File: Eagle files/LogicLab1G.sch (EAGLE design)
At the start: 153 parts, among them IC1 74AHC1G00DBV, IC10 74AHC1G00DBV, IC11 74AHC1G00DBV, IC12 74AHC1G00DBV, IC13 74AHC1G00DBV, IC14 74AHC1G00DBV, IC15 74AHC1G00DBV, IC16 74AHC1G00DBV, IC17 74AHC1G00DBV, IC2 74AHC1G00DBV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

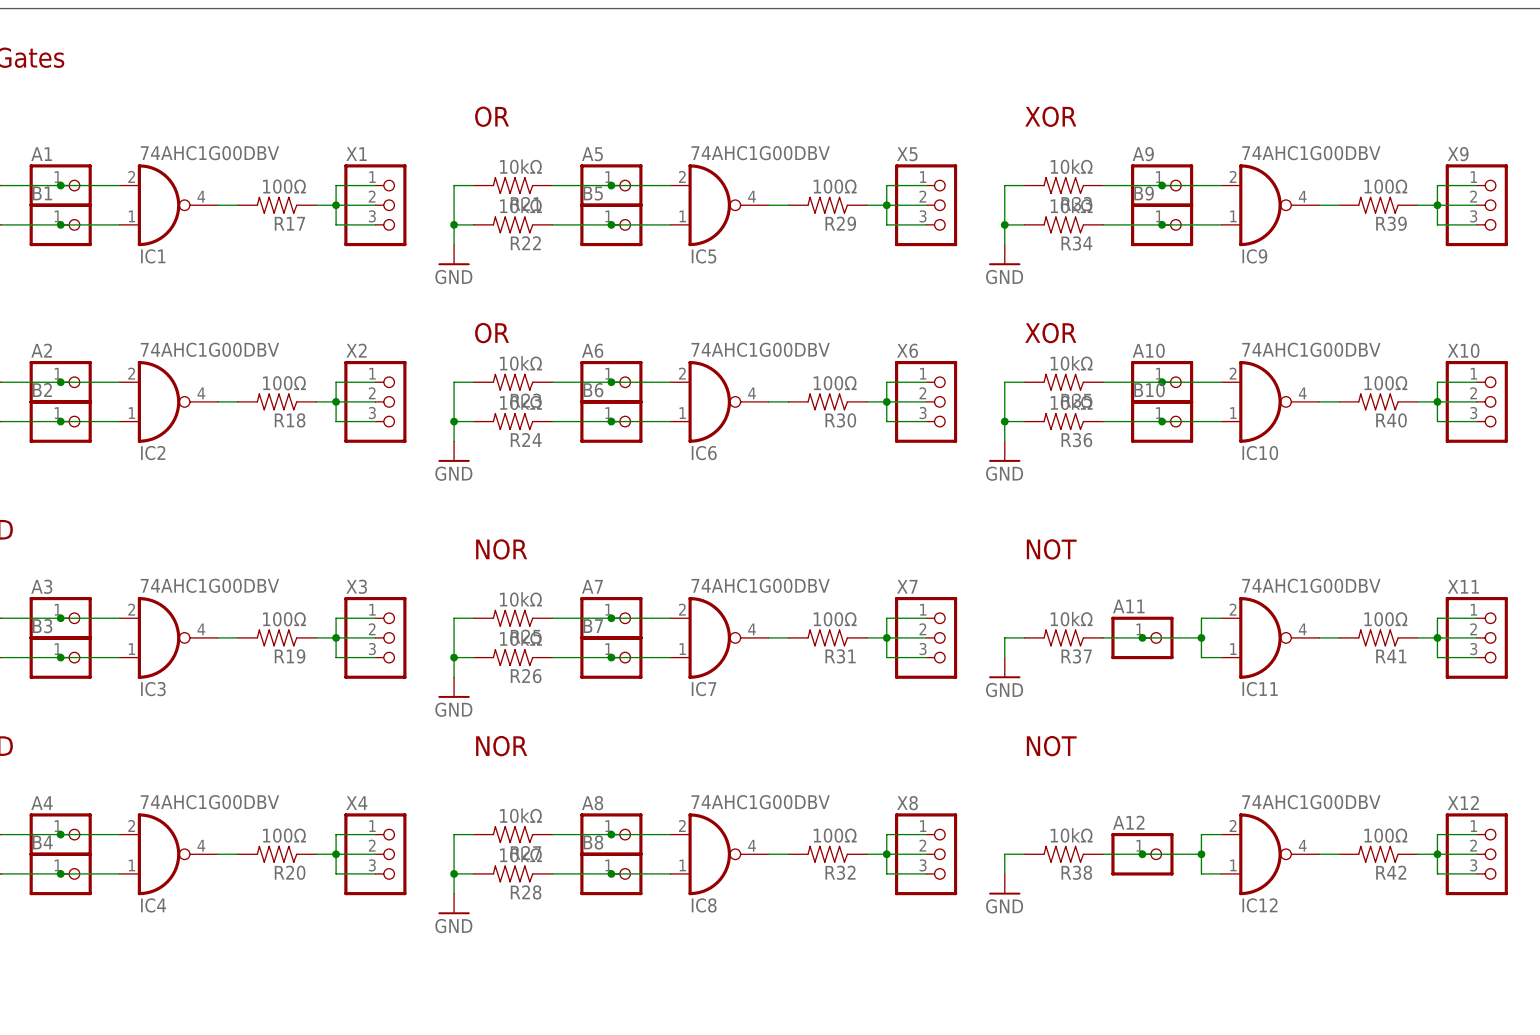
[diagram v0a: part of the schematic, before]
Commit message: Version 1a - 17th June 2024
Corrected the part numbers of the logic gates.
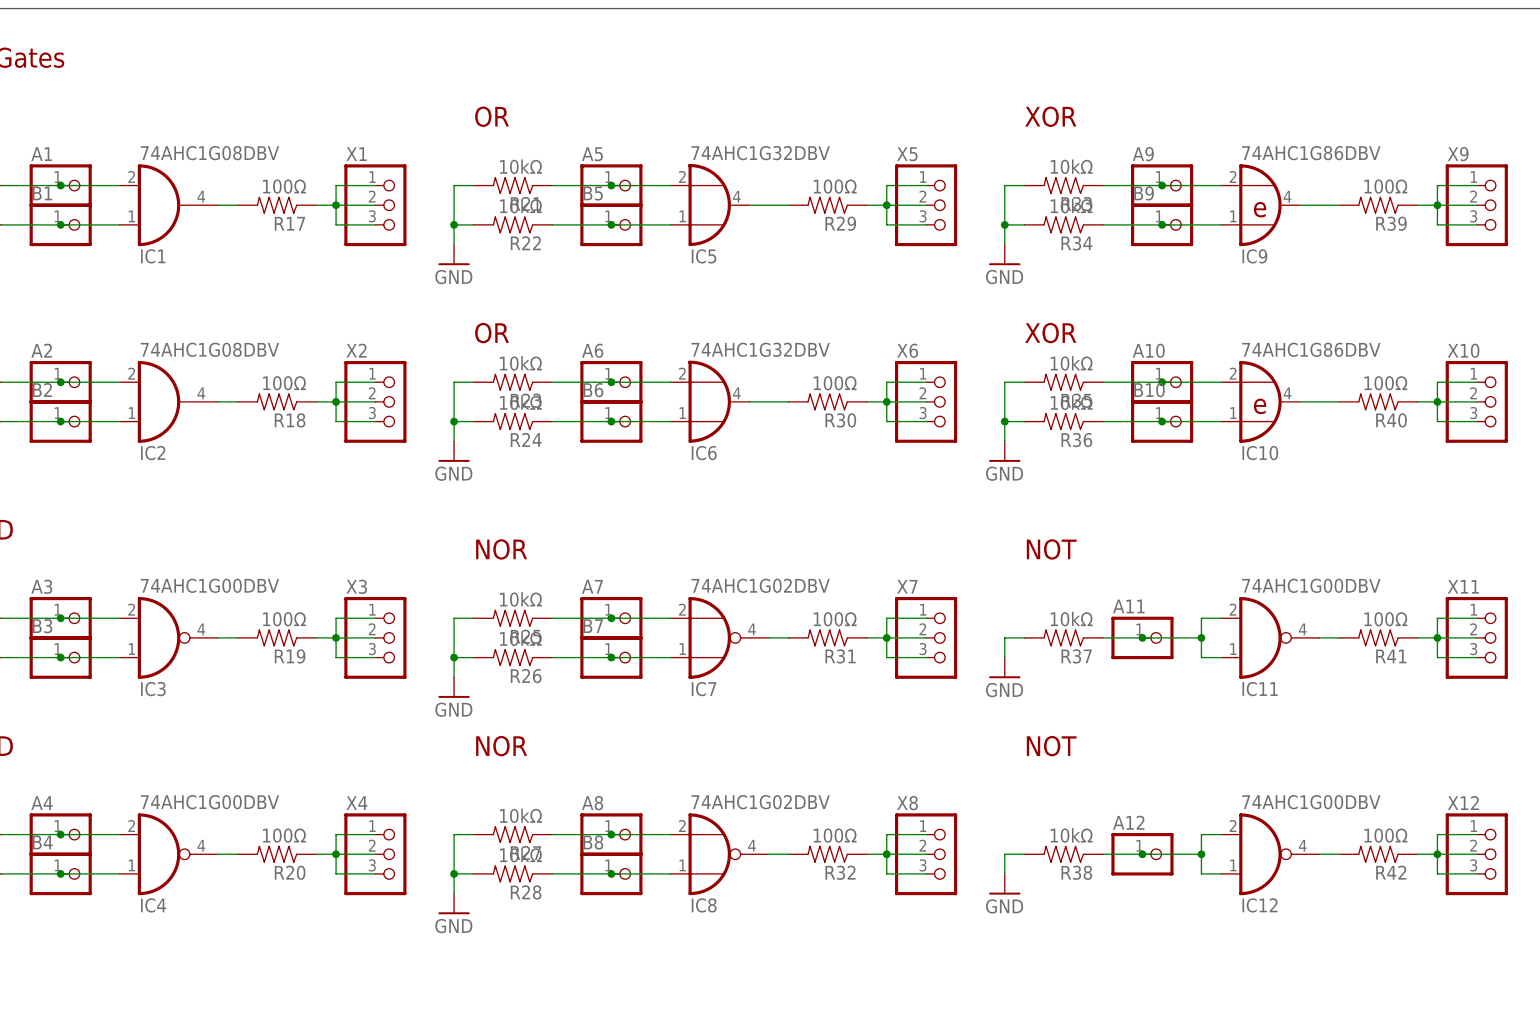
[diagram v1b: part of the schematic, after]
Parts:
- IC1, IC2: value 74AHC1G00DBV -> 74AHC1G08DBV; device 74xx-little-de:74AHC1G00DBV -> 74xx-little-de:74AHC1G08DBV
- IC10, IC9: value 74AHC1G00DBV -> 74AHC1G86DBV; device 74xx-little-de:74AHC1G00DBV -> 74xx-little-de:74AHC1G86DBV
- IC5, IC6: value 74AHC1G00DBV -> 74AHC1G32DBV; device 74xx-little-de:74AHC1G00DBV -> 74xx-little-de:74AHC1G32DBV
- IC7, IC8: value 74AHC1G00DBV -> 74AHC1G02DBV; device 74xx-little-de:74AHC1G00DBV -> 74xx-little-de:74AHC1G02DBV
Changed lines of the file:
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@@
 <part name="J1" library="adafruit" deviceset="1X4" device="-BIG"/>
 <part name="D1" library="SparkFun-DiscreteSemi" deviceset="B340A" device="" value="B340A"/>
-<part name="IC1" library="74xx-little-de" deviceset="74*1G00" device="DBV" technology="AHC"/>
-<part name="IC2" library="74xx-little-de" deviceset="74*1G00" device="DBV" technology="AHC"/>
+<part name="IC1" library="74xx-little-de" deviceset="74*1G08" device="DBV" technology="AHC"/>
+<part name="IC2" library="74xx-little-de" deviceset="74*1G08" device="DBV" technology="AHC"/>
 <part name="IC3" library="74xx-little-de" deviceset="74*1G00" device="DBV" technology="AHC"/>
 <part name="IC4" library="74xx-little-de" deviceset="74*1G00" device="DBV" technology="AHC"/>
-<part name="IC5" library="74xx-little-de" deviceset="74*1G00" device="DBV" technology="AHC"/>
-<part name="IC6" library="74xx-little-de" deviceset="74*1G00" device="DBV" technology="AHC"/>
-<part name="IC7" library="74xx-little-de" deviceset="74*1G00" device="DBV" technology="AHC"/>
-<part name="IC8" library="74xx-little-de" deviceset="74*1G00" device="DBV" technology="AHC"/>
-<part name="IC9" library="74xx-little-de" deviceset="74*1G00" device="DBV" technology="AHC"/>
-<part name="IC10" library="74xx-little-de" deviceset="74*1G00" device="DBV" technology="AHC"/>
+<part name="IC5" library="74xx-little-de" deviceset="74*1G32" device="DBV" technology="AHC"/>
+<part name="IC6" library="74xx-little-de" deviceset="74*1G32" device="DBV" technology="AHC"/>
+<part name="IC7" library="74xx-little-de" deviceset="74*1G02" device="DBV" technology="AHC"/>
+<part name="IC8" library="74xx-little-de" deviceset="74*1G02" device="DBV" technology="AHC"/>
+<part name="IC9" library="74xx-little-de" deviceset="74*1G86" device="DBV" technology="AHC"/>
+<part name="IC10" library="74xx-little-de" deviceset="74*1G86" device="DBV" technology="AHC"/>
 <part name="IC11" library="74xx-little-de" deviceset="74*1G00" device="DBV" technology="AHC"/>
 <part name="IC12" library="74xx-little-de" deviceset="74*1G00" device="DBV" technology="AHC"/>
@@
 <pinref part="IC5" gate="A" pin="O"/>
 <pinref part="R29" gate="G$1" pin="2"/>
-<wire x1="121.92" y1="124.46" x2="124.46" y2="124.46" width="0.1524" layer="91"/>
+<wire x1="119.38" y1="124.46" x2="124.46" y2="124.46" width="0.1524" layer="91"/>
 </segment>
 </net>
@@
 <segment>
 <pinref part="IC6" gate="A" pin="O"/>
-<wire x1="121.92" y1="99.06" x2="124.46" y2="99.06" width="0.1524" layer="91"/>
+<wire x1="119.38" y1="99.06" x2="124.46" y2="99.06" width="0.1524" layer="91"/>
 <pinref part="R30" gate="G$1" pin="2"/>
 </segment>
@@
 <pinref part="IC9" gate="A" pin="O"/>
 <pinref part="R39" gate="G$1" pin="2"/>
-<wire x1="193.04" y1="124.46" x2="195.58" y2="124.46" width="0.1524" layer="91"/>
+<wire x1="190.5" y1="124.46" x2="195.58" y2="124.46" width="0.1524" layer="91"/>
 </segment>
 </net>
@@
 <pinref part="IC10" gate="A" pin="O"/>
 <pinref part="R40" gate="G$1" pin="2"/>
-<wire x1="193.04" y1="99.06" x2="195.58" y2="99.06" width="0.1524" layer="91"/>
-</segment>
-</net>
+<wire x1="190.5" y1="99.06" x2="195.58" y2="99.06" width="0.1524" layer="91"/>
+</segment>
+</net>
